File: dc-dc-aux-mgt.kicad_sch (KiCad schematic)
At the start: 42 parts, among them U19 MPM54304GMN, U25 PAC1720-1, U3 PAC1720-1

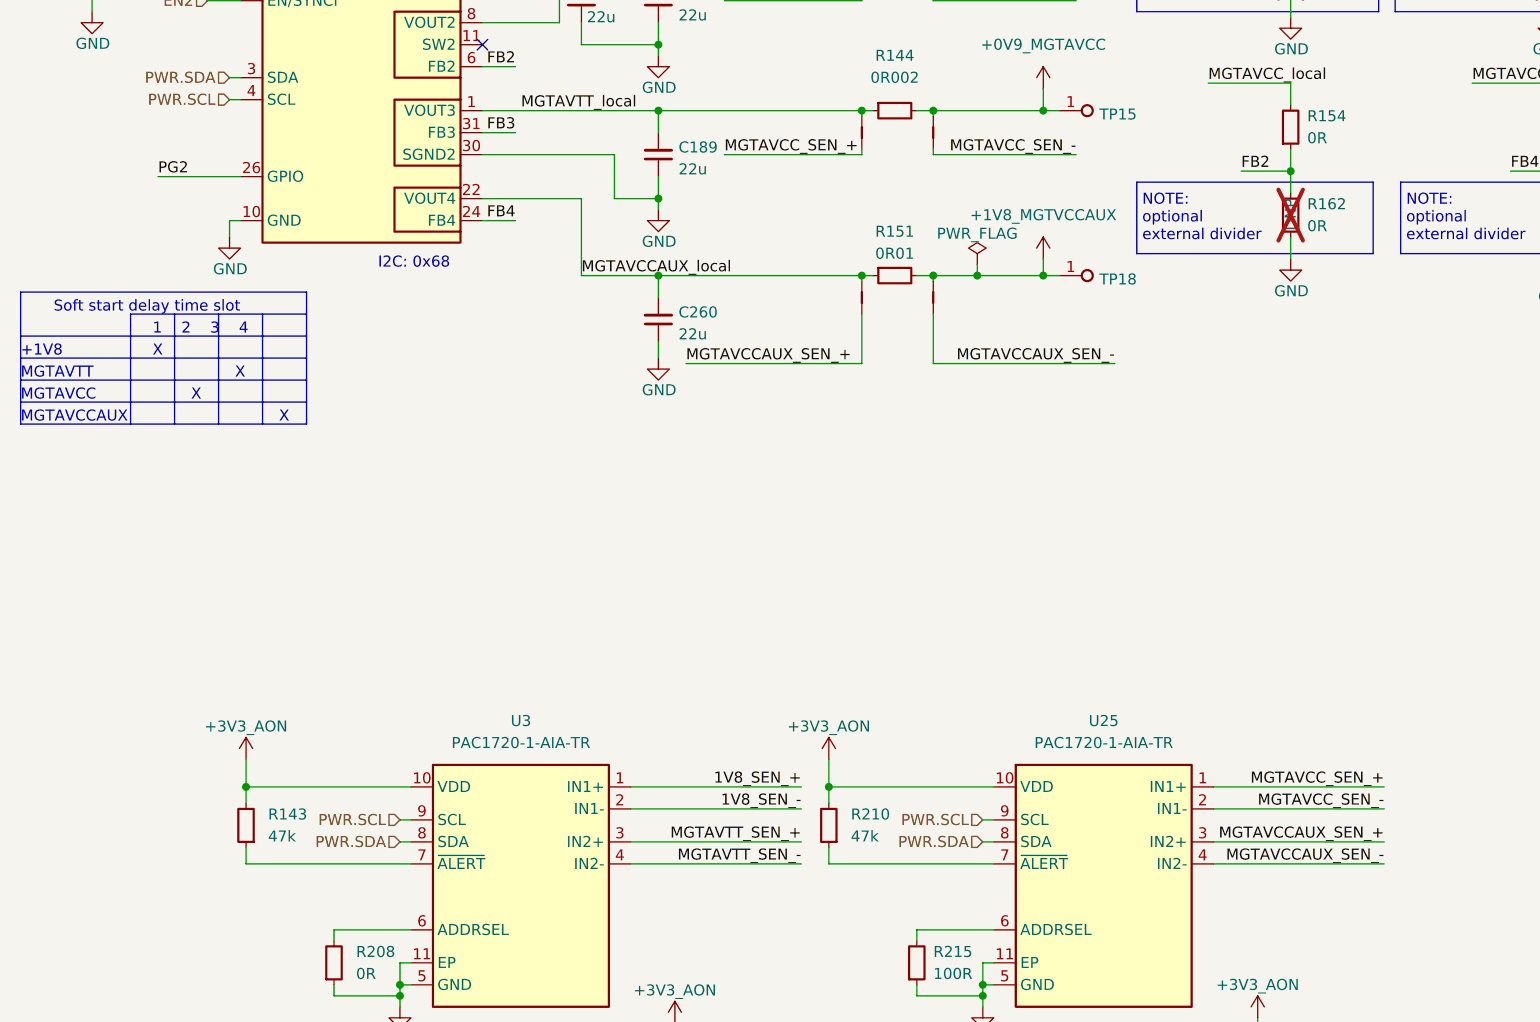
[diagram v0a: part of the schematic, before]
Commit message: [#66727] Continue routing low speed signals
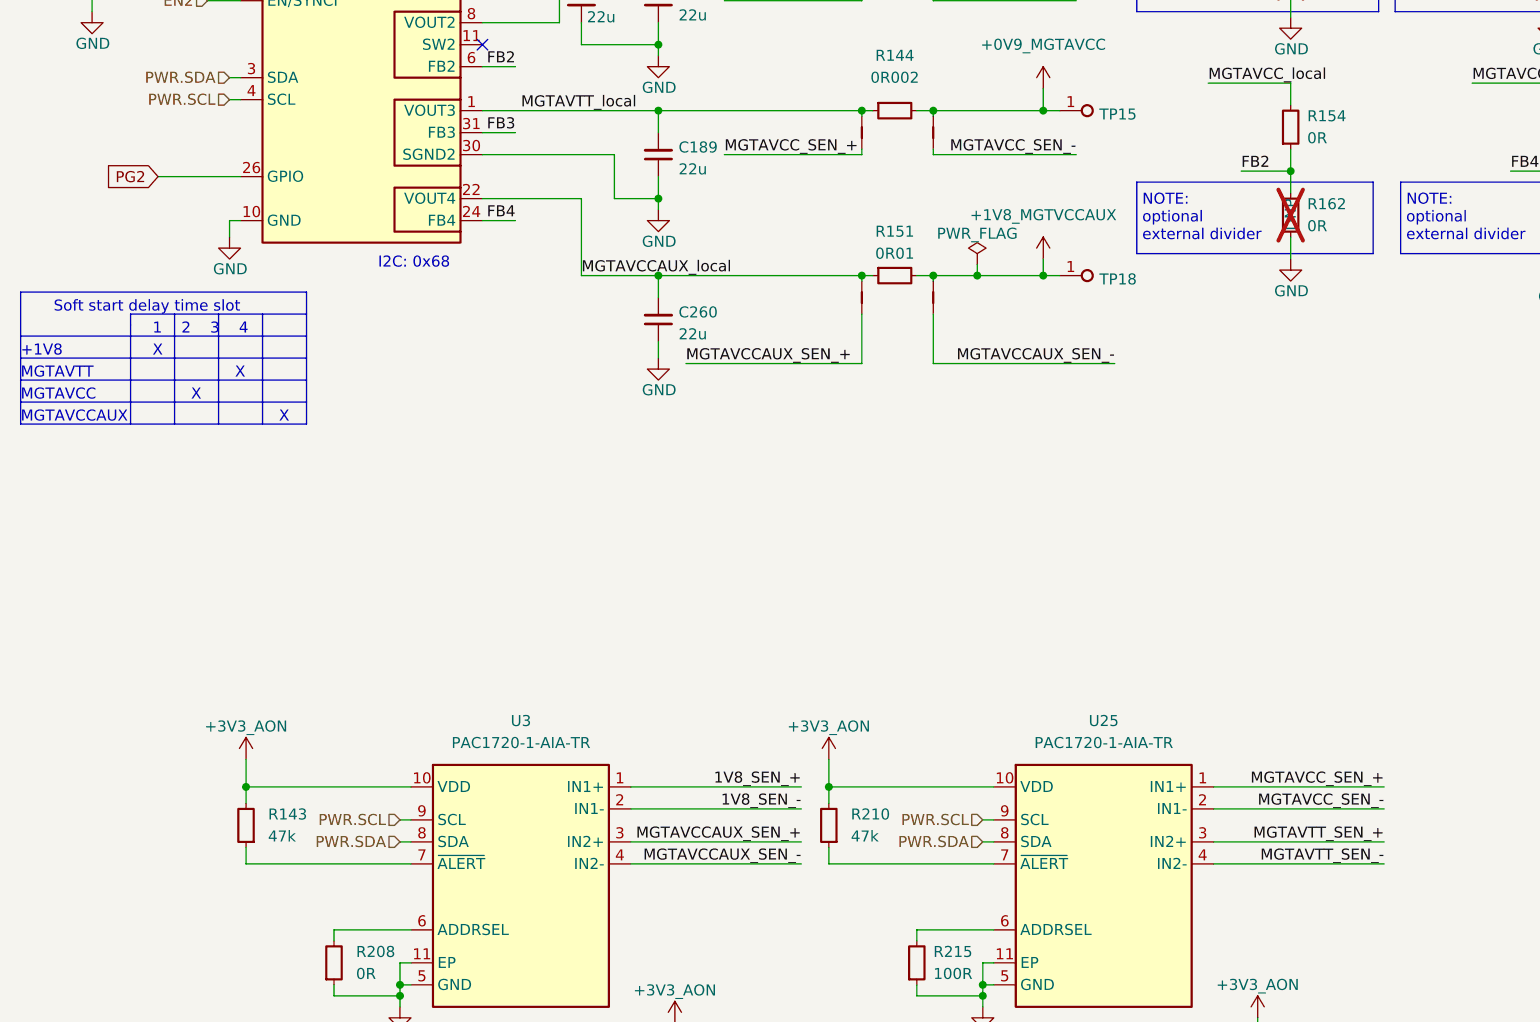
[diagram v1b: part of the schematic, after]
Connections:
- net MGTAVCCAUX_SEN_+: now also U3.3 (IN2+); no longer U25.3 (IN2+)
- net MGTAVCCAUX_SEN_-: now also U3.4 (IN2-); no longer U25.4 (IN2-)
- net MGTAVTT_SEN_+: now also U25.3 (IN2+); no longer U3.3 (IN2+)
- net MGTAVTT_SEN_-: now also U25.4 (IN2-); no longer U3.4 (IN2-)
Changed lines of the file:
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@@
     (effects (font (size 1.27 1.27)) (justify left bottom))
   )
-  (label "MGTAVTT_SEN_-" (at 147.32 189.23 180) (fields_autoplaced)
+  (label "MGTAVTT_SEN_-" (at 214.63 189.23 180) (fields_autoplaced)
     (effects (font (size 1.27 1.27)) (justify right bottom))
   )
-  (label "MGTAVTT_SEN_+" (at 147.32 186.69 180) (fields_autoplaced)
+  (label "MGTAVTT_SEN_+" (at 214.63 186.69 180) (fields_autoplaced)
     (effects (font (size 1.27 1.27)) (justify right bottom))
   )
@@
     (effects (font (size 1.27 1.27)) (justify right bottom))
   )
-  (label "PG2" (at 73.025 109.855 0) (fields_autoplaced)
-    (effects (font (size 1.27 1.27)) (justify left bottom))
-  )
-  (label "MGTAVCCAUX_SEN_+" (at 214.63 186.69 180) (fields_autoplaced)
+  (label "MGTAVCCAUX_SEN_+" (at 147.32 186.69 180) (fields_autoplaced)
     (effects (font (size 1.27 1.27)) (justify right bottom))
   )
@@
     (effects (font (size 1.27 1.27)) (justify left bottom))
   )
-  (label "MGTAVCCAUX_SEN_-" (at 214.63 189.23 180) (fields_autoplaced)
+  (label "MGTAVCCAUX_SEN_-" (at 147.32 189.23 180) (fields_autoplaced)
     (effects (font (size 1.27 1.27)) (justify right bottom))
   )
@@
     (effects (font (size 1.27 1.27)) (justify right bottom))
   )
+  (global_label "PG2" (shape input) (at 73.025 109.855 180) (fields_autoplaced)
+    (effects (font (size 1.27 1.27)) (justify right))
+    (property "Intersheetrefs" "${INTERSHEET_REFS}" (at 66.9445 109.855 0)
+      (effects (font (size 1.27 1.27)) (justify right))
+    )
+  )
   (hierarchical_label "PWR.SDA" (shape input) (at 81.28 98.425 180) (fields_autoplaced)

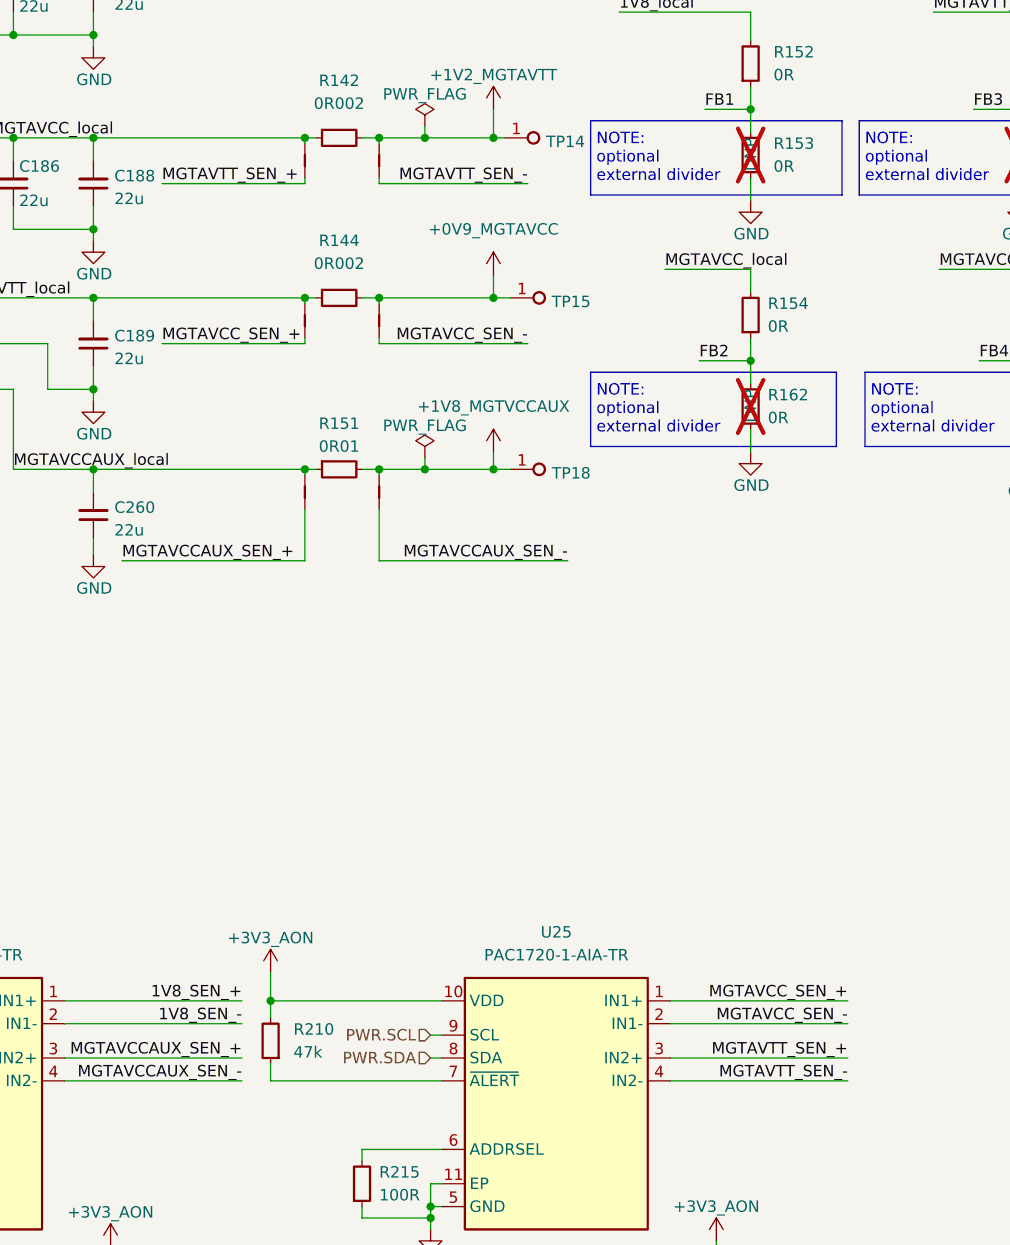
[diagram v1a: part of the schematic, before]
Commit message: [#67532] Clean DRC. Optimize power planes, EMC concept and LS/HS routing
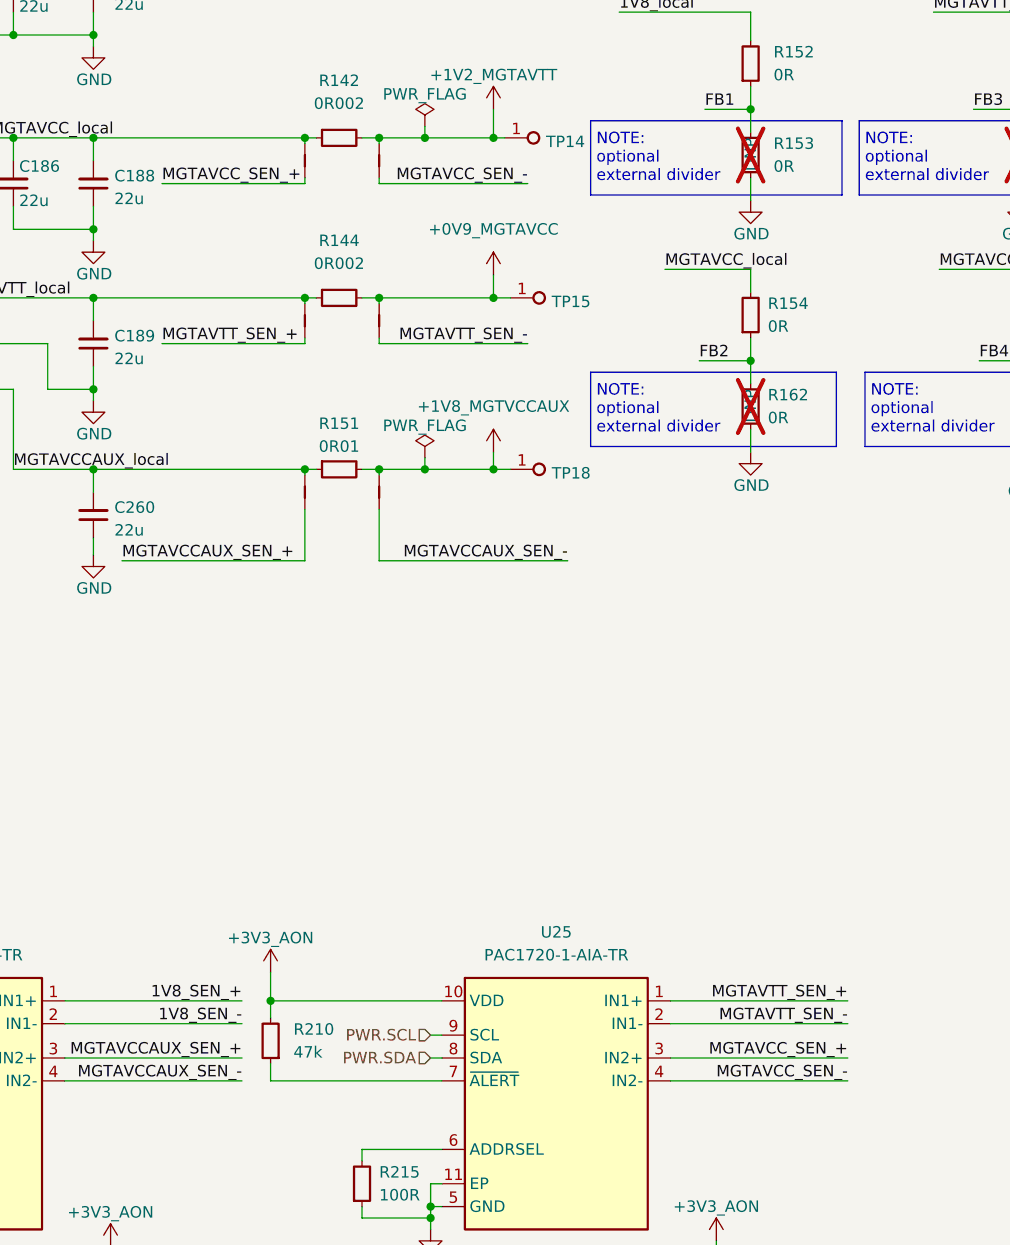
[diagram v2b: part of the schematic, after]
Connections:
- net MGTAVCC_SEN_+: now also NT2.1, U25.3 (IN2+); no longer NT3.1, U25.1 (IN1+)
- net MGTAVCC_SEN_-: now also NT10.1, U25.4 (IN2-); no longer NT11.1, U25.2 (IN1-)
- net MGTAVTT_SEN_+: now also NT3.1, U25.1 (IN1+); no longer NT2.1, U25.3 (IN2+)
- net MGTAVTT_SEN_-: now also NT11.1, U25.2 (IN1-); no longer NT10.1, U25.4 (IN2-)
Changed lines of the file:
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@@
     (effects (font (size 1.27 1.27)) (justify left bottom))
   )
-  (label "MGTAVTT_SEN_-" (at 179.07 89.535 180) (fields_autoplaced)
+  (label "MGTAVTT_SEN_-" (at 179.07 107.315 180) (fields_autoplaced)
     (effects (font (size 1.27 1.27)) (justify right bottom))
   )
@@
     (effects (font (size 1.27 1.27)) (justify left bottom))
   )
-  (label "MGTAVTT_SEN_-" (at 214.63 189.23 180) (fields_autoplaced)
+  (label "MGTAVTT_SEN_-" (at 214.63 182.88 180) (fields_autoplaced)
     (effects (font (size 1.27 1.27)) (justify right bottom))
   )
-  (label "MGTAVTT_SEN_+" (at 214.63 186.69 180) (fields_autoplaced)
+  (label "MGTAVTT_SEN_+" (at 214.63 180.34 180) (fields_autoplaced)
     (effects (font (size 1.27 1.27)) (justify right bottom))
   )
@@
     (effects (font (size 1.27 1.27)) (justify left bottom))
   )
-  (label "MGTAVCC_SEN_-" (at 214.63 182.88 180) (fields_autoplaced)
+  (label "MGTAVCC_SEN_-" (at 214.63 189.23 180) (fields_autoplaced)
     (effects (font (size 1.27 1.27)) (justify right bottom))
   )
@@
     (effects (font (size 1.27 1.27)) (justify left bottom))
   )
-  (label "MGTAVCC_SEN_+" (at 138.43 107.315 0) (fields_autoplaced)
+  (label "MGTAVCC_SEN_+" (at 138.43 89.535 0) (fields_autoplaced)
     (effects (font (size 1.27 1.27)) (justify left bottom))
   )
@@
     (effects (font (size 1.27 1.27)) (justify left bottom))
   )
-  (label "MGTAVCC_SEN_+" (at 214.63 180.34 180) (fields_autoplaced)
+  (label "MGTAVCC_SEN_+" (at 214.63 186.69 180) (fields_autoplaced)
     (effects (font (size 1.27 1.27)) (justify right bottom))
   )
@@
     (effects (font (size 1.27 1.27)) (justify left bottom))
   )
-  (label "MGTAVTT_SEN_+" (at 138.43 89.535 0) (fields_autoplaced)
+  (label "MGTAVTT_SEN_+" (at 138.43 107.315 0) (fields_autoplaced)
     (effects (font (size 1.27 1.27)) (justify left bottom))
   )
-  (label "MGTAVCC_SEN_-" (at 179.07 107.315 180) (fields_autoplaced)
+  (label "MGTAVCC_SEN_-" (at 179.07 89.535 180) (fields_autoplaced)
     (effects (font (size 1.27 1.27)) (justify right bottom))
   )

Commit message: [#67725] Update vccaux power supply
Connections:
- net MGTAVCC_SEN_+: now also NT3.1; no longer NT2.1
- net MGTAVCC_SEN_-: now also NT11.1; no longer NT10.1
- net MGTAVCC_local: now also C189.2, NT3.2, R144.1, U19.1 (VOUT3), U19.32 (VOUT3); no longer C186.2, C188.2, NT2.2, R142.1, U19.8 (VOUT2), U19.9 (VOUT2)
- net MGTAVTT_SEN_+: now also NT2.1; no longer NT3.1
- net MGTAVTT_SEN_-: now also NT10.1; no longer NT11.1
- net MGTAVTT_local: now also C186.2, C188.2, NT2.2, R142.1, U19.8 (VOUT2), U19.9 (VOUT2); no longer C189.2, NT3.2, R144.1, U19.1 (VOUT3), U19.32 (VOUT3)
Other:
- note added: "Current sense monitors"
- moved on the sheet: C171, C172, C182, C183, C186, C187, C188, C189, C199, C214, C260, R141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
